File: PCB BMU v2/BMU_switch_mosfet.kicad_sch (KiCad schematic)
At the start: 18 parts, among them Q1 BC337, Q10 IRF4905STRLPBF, Q2 IRF4905STRLPBF, Q3 IRF4905STRLPBF, Q4 IRF4905STRLPBF, Q5 IRF4905STRLPBF, Q6 BC337, Q7 IRF4905STRLPBF, Q8 IRF4905STRLPBF, Q9 IRF4905STRLPBF, U1 HX PZ2.54-1X2P ZZ, U2 ZX-IDC2.54-2-5PZZ, U3 ZX-IDC2.54-2-5PZZ

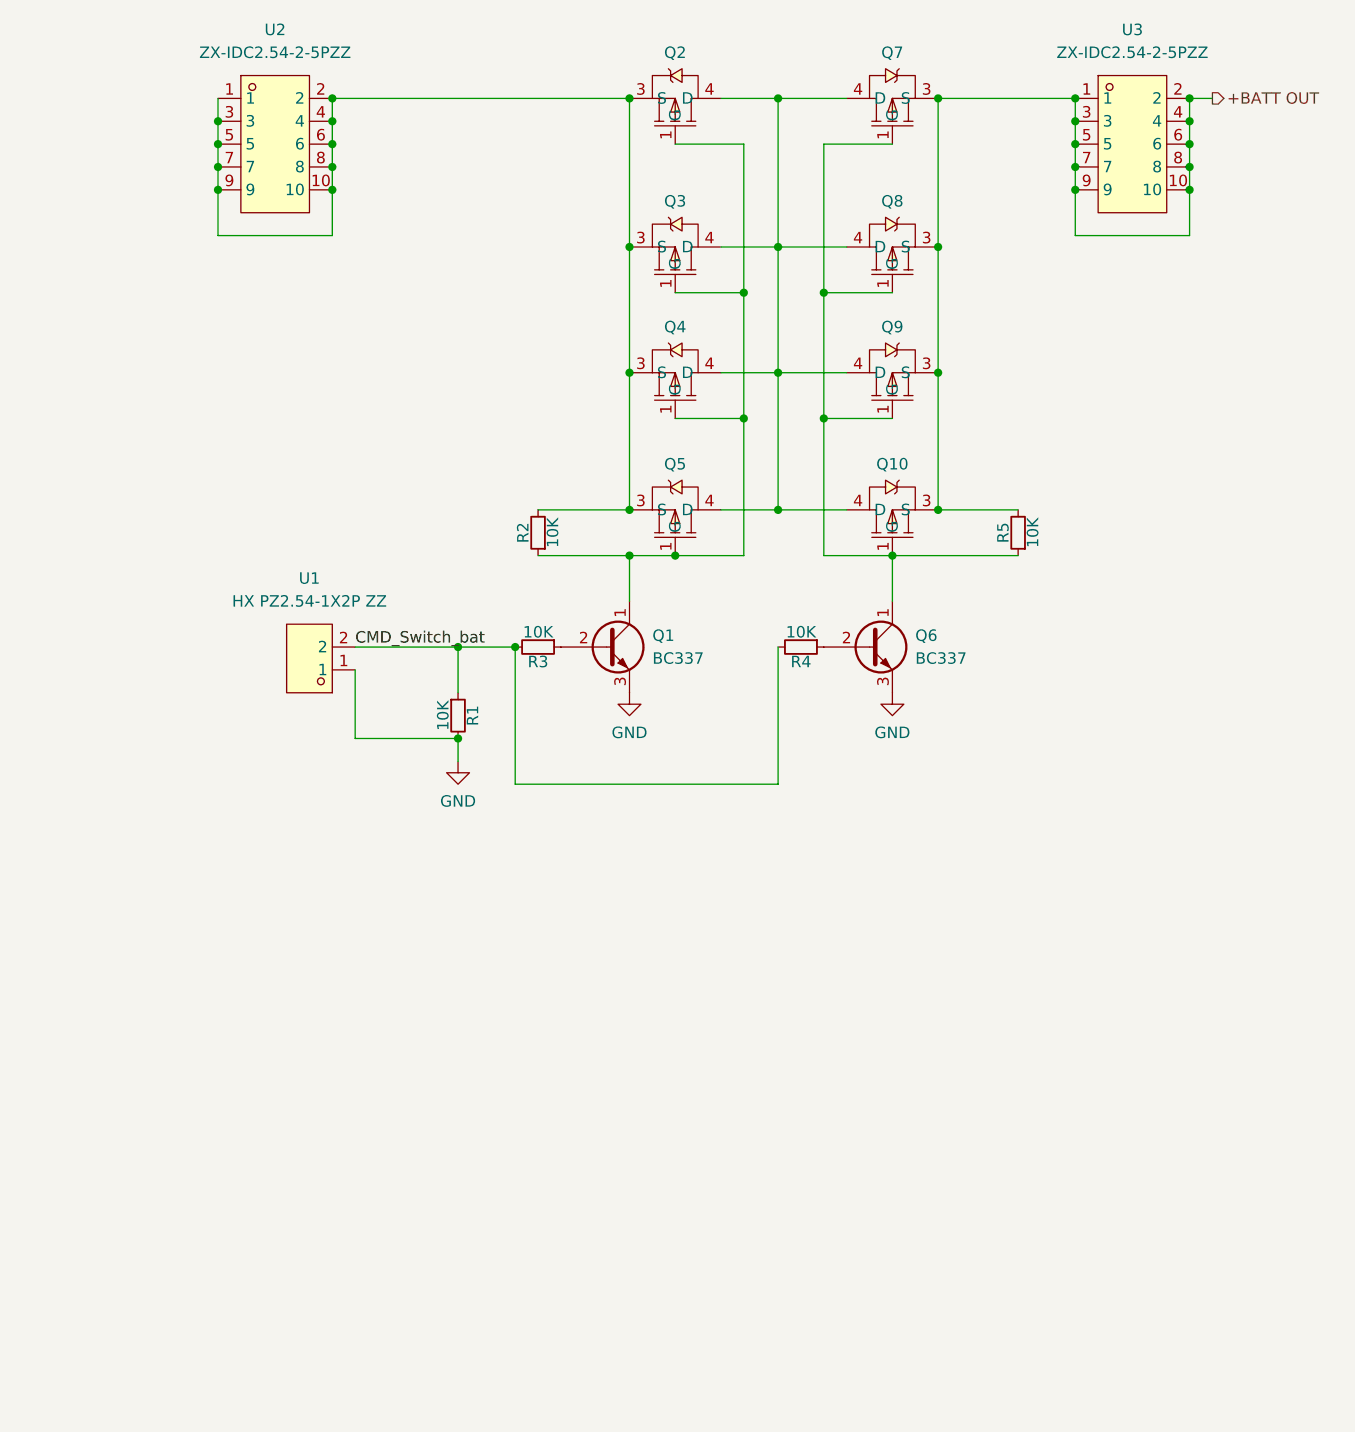
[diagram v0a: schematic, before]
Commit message: add Ampère/Houre calculation
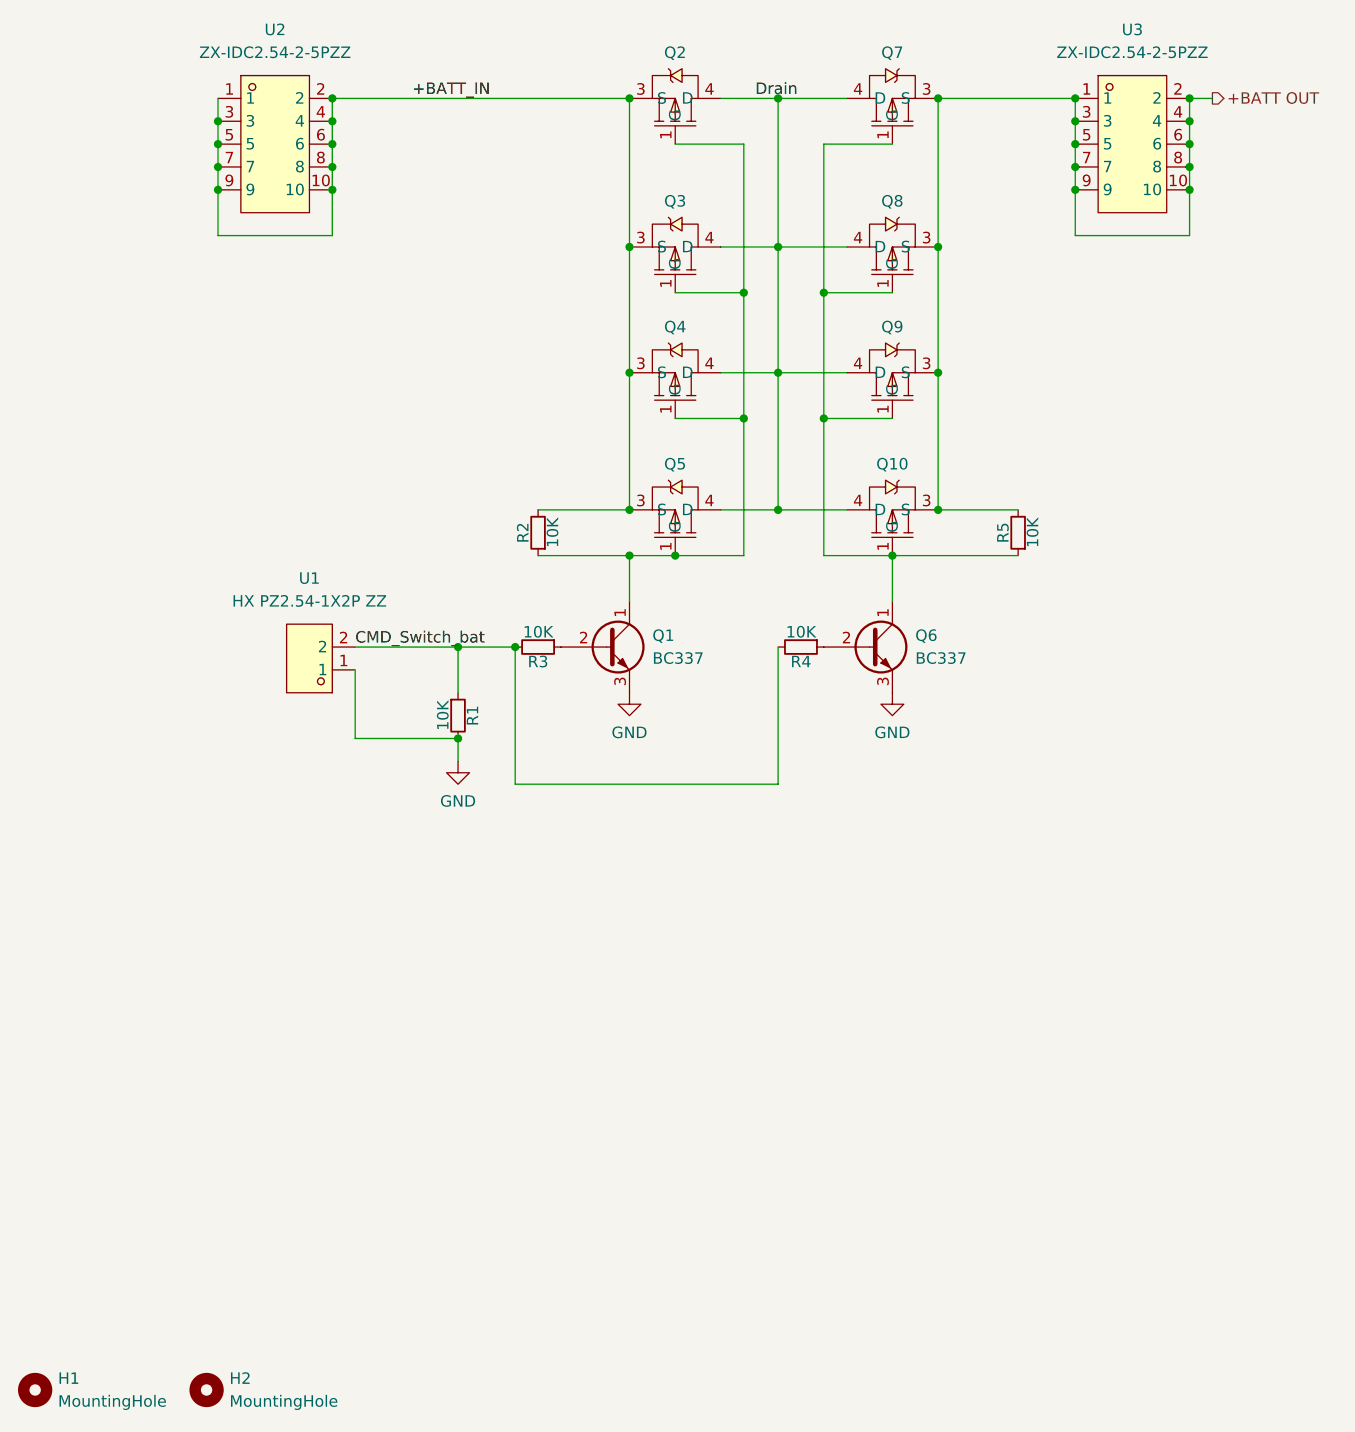
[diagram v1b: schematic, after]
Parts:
- added H1, H2: MountingHole, MountingHole:MountingHole_2.7mm_M2.5, symbol Mechanical:MountingHole
- Q1, Q6: footprint Package_TO_SOT_THT:TO-92_Inline -> Package_TO_SOT_SMD:SOT-23-3
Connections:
- net Drain: now reaches Q10.4 (D), Q2.4 (D), Q3.4 (D), Q4.4 (D), Q5.4 (D), Q7.4 (D), Q8.4 (D), Q9.4 (D)
- net +BATT_IN: now reaches Q2.3 (S), Q3.3 (S), Q4.3 (S), Q5.3 (S), R2.2, U2.1, U2.10, U2.2, U2.3, U2.4, U2.5, U2.6, U2.7, U2.8, U2.9
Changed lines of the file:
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@@
+		)
+	)
+	(label "Drain"
+		(at 101.6 46.99 0)
+		(fields_autoplaced yes)
+		(effects
+			(font
+				(size 1.27 1.27)
+			)
+			(justify left bottom)
+		)
+	)
+	(label "+BATT_IN"
+		(at 63.5 46.99 0)
+		(fields_autoplaced yes)
+		(effects
+			(font
+				(size 1.27 1.27)
+			)
+			(justify left bottom)
 		)
 	)
@@
 			)
 		)
-		(property "Footprint" "Package_TO_SOT_THT:TO-92_Inline"
+		(property "Footprint" "Package_TO_SOT_SMD:SOT-23-3"
 			(at 90.17 109.855 0)
 			(effects
@@
 			)
 		)
-		(property "Footprint" "Package_TO_SOT_THT:TO-92_Inline"
+		(property "Footprint" "Package_TO_SOT_SMD:SOT-23-3"
 			(at 119.38 109.855 0)
 			(effects
@@
 	)
 	(symbol
+		(lib_id "Mechanical:MountingHole")
+		(at 21.59 190.5 0)
+		(unit 1)
+		(exclude_from_sim yes)
+		(in_bom no)
+		(on_board yes)
+		(dnp no)
+		(fields_autoplaced yes)
+		(property "Reference" "H1"
+			(at 24.13 189.2299 0)
+			(effects
+				(font
+					(size 1.27 1.27)
+				)
+				(justify left)
+			)
+		)
+		(property "Value" "MountingHole"
+			(at 24.13 191.7699 0)
+			(effects
+				(font
+					(size 1.27 1.27)
+				)
+				(justify left)
+			)
+		)
+		(property "Footprint" "MountingHole:MountingHole_2.7mm_M2.5"
+			(at 21.59 190.5 0)
+			(effects
+				(font
+					(size 1.27 1.27)
+				)
+				(hide yes)
+			)
+		)
+		(property "Datasheet" "~"
+			(at 21.59 190.5 0)
+			(effects
+				(font
+					(size 1.27 1.27)
+				)
+				(hide yes)
+			)
+		)
+		(property "Description" "Mounting Hole without connection"
+			(at 21.59 190.5 0)
+			(effects
+				(font
+					(size 1.27 1.27)
+				)
+				(hide yes)
+			)
+		)
+		(instances
+			(project ""
+				(path "/40c3f397-d07f-488b-b615-517efc4a5c8c"
+					(reference "H1")
+					(unit 1)
+				)
+			)
+		)
+	)
+	(symbol
 		(lib_id "power:GND")
 		(at 68.58 120.65 0)
@@
 					(unit 1)
 				)
+			)
+		)
+	)
+	(symbol
+		(lib_id "Mechanical:MountingHole")
+		(at 40.64 190.5 0)
+		(unit 1)
+		(exclude_from_sim yes)
+		(in_bom no)
+		(on_board yes)
+		(dnp no)
+		(fields_autoplaced yes)
+		(property "Reference" "H2"
+			(at 43.18 189.2299 0)
+			(effects
+				(font
+					(size 1.27 1.27)
+				)
+				(justify left)
+			)
+		)
+		(property "Value" "MountingHole"
+			(at 43.18 191.7699 0)
+			(effects
+				(font
+					(size 1.27 1.27)
+				)
+				(justify left)
+			)
+		)
+		(property "Footprint" "MountingHole:MountingHole_2.7mm_M2.5"
+			(at 40.64 190.5 0)
+			(effects
+				(font
+					(size 1.27 1.27)
+				)
+				(hide yes)
+			)
+		)
+		(property "Datasheet" "~"
+			(at 40.64 190.5 0)
+			(effects
+				(font
+					(size 1.27 1.27)
+				)
+				(hide yes)
+			)
+		)
+		(property "Description" "Mounting Hole without connection"
+			(at 40.64 190.5 0)
+			(effects
+				(font
+					(size 1.27 1.27)
+				)
+				(hide yes)
+			)
+		)
+		(instances
+			(project "BMU_switch_mosfet"
+				(path "/40c3f397-d07f-488b-b615-517efc4a5c8c"
+					(reference "H2")
+					(unit 1)
+				)
